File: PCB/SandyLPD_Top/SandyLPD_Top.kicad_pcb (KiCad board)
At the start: 2 copper layers, 30.3 x 23 mm, 22 parts

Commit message: シルク位置調整 #20
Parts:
- moved REF** 5.73 mm to (128.3, 38.3), turned to -90 degrees
- moved REF** 4.31 mm to (145.7, 36.4), turned to 90 degrees
- moved REF** 0.95 mm to (121.0, 38.9)
- moved REF** 0.85 mm to (143.6, 55.0)
- moved REF** 0.83 mm to (143.7, 55.0)
- moved REF** 0.50 mm to (143.7, 39.6)
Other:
- board text added: "L Back"
- board text added: "R Back"
- board text removed: "L 左 Back"
- board text removed: "R 右 Back"
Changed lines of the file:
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@@
 		(locked yes)
 		(layer "F.Cu")
-		(at 143.225342 55.773449)
+		(at 143.645755 55.032837)
 		(property "Reference" "REF**"
 			(at 0 0.5 0)
@@
 		(fp_arc
 			(start 2.475824 -5.107131)
-			(mid 1.4 -5.3)
+			(mid 1.399999 -5.299999)
 			(end 0.555319 -5.993622)
 			(stroke
@@
 		(locked yes)
 		(layer "F.Cu")
-		(at 120.204016 38.385937 -90)
+		(at 121.021287 38.862502 -90)
 		(property "Reference" "REF**"
 			(at 0 0.5 90)
@@
 		(fp_arc
 			(start 2.475824 -5.107131)
-			(mid 1.399999 -5.299999)
+			(mid 1.4 -5.3)
 			(end 0.555319 -5.993622)
 			(stroke
@@
 		(locked yes)
 		(layer "F.Cu")
-		(at 142.225342 38.973449)
+		(at 145.656604 36.370873 90)
 		(property "Reference" "REF**"
-			(at 0 0.5 0)
+			(at 0 0.5 90)
 			(layer "Cmts.User")
 			(effects
@@
 		)
 		(property "Value" "ICON_Screw_Long_Medium"
-			(at 0 -0.5 0)
+			(at 0 -0.5 90)
 			(layer "F.Fab")
 			(effects
@@
 		)
 		(property "Footprint" "locallib:ICON_Screw_Long_Medium"
-			(at 0 0 0)
+			(at 0 0 90)
 			(layer "F.Fab")
 			(hide yes)
@@
 		)
 		(property "Datasheet" ""
-			(at 0 0 0)
+			(at 0 0 90)
 			(layer "F.Fab")
 			(hide yes)
@@
 		)
 		(property "Description" ""
-			(at 0 0 0)
+			(at 0 0 90)
 			(layer "F.Fab")
 			(hide yes)
@@
 		(attr through_hole board_only)
 		(fp_line
-			(start -1.175 -1.6)
-			(end -0.125 -1.6)
+			(start 1.200117 -6.018574)
+			(end 2.000117 -5.318574)
 			(stroke
 				(width 0.06)
@@
 		)
 		(fp_line
-			(start -0.925 -2.05)
-			(end 0.125 -2.05)
+			(start 1.950117 -5.818574)
+			(end 1.200117 -5.568574)
 			(stroke
 				(width 0.06)
@@
 		)
 		(fp_line
-			(start -0.675 -2.5)
-			(end 0.375 -2.5)
+			(start 0.95 -5.55)
+			(end -1.3 -1.5)
 			(stroke
-				(width 0.06)
+				(width 0.12)
 				(type solid)
 			)
@@
 		)
 		(fp_line
-			(start -0.425 -2.95)
-			(end 0.625 -2.95)
+			(start 1.85 -5.1)
+			(end -0.35 -1.1)
 			(stroke
-				(width 0.06)
+				(width 0.12)
 				(type solid)
 			)
@@
 		)
 		(fp_line
-			(start -0.175 -3.45)
-			(end 0.875 -3.45)
+			(start 0.675 -4.95)
+			(end 1.725 -4.95)
 			(stroke
 				(width 0.06)
@@
 		)
 		(fp_line
-			(start 0.125 -3.95)
-			(end 1.175 -3.95)
+			(start 0.375 -4.45)
+			(end 1.425 -4.45)
 			(stroke
 				(width 0.06)
@@
 		)
 		(fp_line
-			(start 0.375 -4.45)
-			(end 1.425 -4.45)
+			(start 0.125 -3.95)
+			(end 1.175 -3.95)
 			(stroke
 				(width 0.06)
@@
 		)
 		(fp_line
-			(start 0.675 -4.95)
-			(end 1.725 -4.95)
+			(start -0.175 -3.45)
+			(end 0.875 -3.45)
 			(stroke
 				(width 0.06)
@@
 		)
 		(fp_line
-			(start 0.95 -5.55)
-			(end -1.3 -1.5)
+			(start -0.425 -2.95)
+			(end 0.625 -2.95)
 			(stroke
-				(width 0.12)
+				(width 0.06)
 				(type solid)
 			)
@@
 		)
 		(fp_line
-			(start 1.200117 -6.018574)
-			(end 2.000117 -5.318574)
+			(start -0.675 -2.5)
+			(end 0.375 -2.5)
 			(stroke
 				(width 0.06)
@@
 		)
 		(fp_line
-			(start 1.85 -5.1)
-			(end -0.35 -1.1)
+			(start -0.925 -2.05)
+			(end 0.125 -2.05)
 			(stroke
-				(width 0.12)
+				(width 0.06)
 				(type solid)
 			)
@@
 		)
 		(fp_line
-			(start 1.950117 -5.818574)
-			(end 1.200117 -5.568574)
+			(start -1.175 -1.6)
+			(end -0.125 -1.6)
 			(stroke
 				(width 0.06)
@@
 		)
 		(fp_arc
-			(start -0.35 -1.1)
-			(mid -0.918136 -1.068963)
-			(end -1.308578 -1.482842)
+			(start 0.665318 -6.21362)
+			(mid 1.74926 -6.077071)
+			(end 2.5615 -5.346425)
 			(stroke
 				(width 0.12)
@@
 		)
 		(fp_arc
-			(start 0.665318 -6.21362)
-			(mid 1.74926 -6.077071)
-			(end 2.5615 -5.346425)
+			(start 2.557784 -5.343159)
+			(mid 2.58557 -5.201266)
+			(end 2.475824 -5.107132)
 			(stroke
 				(width 0.12)
-				(type solid)
+				(type default)
 			)
 			(layer "F.SilkS")
@@
 		(fp_arc
 			(start 2.475824 -5.107131)
-			(mid 1.4 -5.3)
+			(mid 1.399999 -5.299999)
 			(end 0.555319 -5.993622)
 			(stroke
@@
 		)
 		(fp_arc
-			(start 2.557784 -5.343159)
-			(mid 2.58557 -5.201266)
-			(end 2.475824 -5.107132)
+			(start -0.35 -1.1)
+			(mid -0.918136 -1.068963)
+			(end -1.308578 -1.482842)
 			(stroke
 				(width 0.12)
-				(type default)
+				(type solid)
 			)
 			(layer "F.SilkS")
@@
 	)
 	(footprint "locallib:ICON_Screw_Long_Medium"
+		(locked yes)
 		(layer "B.Cu")
-		(at 126.110278 43.573449 180)
+		(at 128.264501 38.267183 -90)
 		(property "Reference" "REF**"
-			(at 0 -0.5 0)
+			(at 0 -0.5 90)
 			(layer "Cmts.User")
 			(effects
@@
 		)
 		(property "Value" "ICON_Screw_Long_Medium"
-			(at 0 0.5 0)
+			(at 0 0.5 90)
 			(layer "B.Fab")
 			(effects
@@
 		)
 		(property "Footprint" "locallib:ICON_Screw_Long_Medium"
-			(at 0 0 0)
+			(at 0 0 90)
 			(layer "B.Fab")
 			(hide yes)
@@
 		)
 		(property "Datasheet" ""
-			(at 0 0 0)
+			(at 0 0 90)
 			(layer "B.Fab")
 			(hide yes)
@@
 		)
 		(property "Description" ""
-			(at 0 0 0)
+			(at 0 0 90)
 			(layer "B.Fab")
 			(hide yes)
@@
 		(attr through_hole board_only)
 		(fp_line
-			(start 2.000117 5.318574)
-			(end 1.200117 6.018574)
+			(start 1.200117 5.568574)
+			(end 1.950117 5.818574)
 			(stroke
 				(width 0.06)
@@
 		)
 		(fp_line
-			(start 1.725 4.95)
-			(end 0.675 4.95)
+			(start 2.000117 5.318574)
+			(end 1.200117 6.018574)
 			(stroke
 				(width 0.06)
@@
 		)
 		(fp_line
-			(start 1.425 4.45)
-			(end 0.375 4.45)
+			(start 1.725 4.95)
+			(end 0.675 4.95)
 			(stroke
 				(width 0.06)
@@
 		)
 		(fp_line
-			(start 1.200117 5.568574)
-			(end 1.950117 5.818574)
+			(start 1.425 4.45)
+			(end 0.375 4.45)
 			(stroke
 				(width 0.06)
@@
 		)
 		(fp_line
-			(start -0.35 1.1)
-			(end 1.85 5.1)
+			(start -1.3 1.5)
+			(end 0.95 5.55)
 			(stroke
 				(width 0.12)
@@
 		)
 		(fp_line
-			(start -1.3 1.5)
-			(end 0.95 5.55)
+			(start -0.35 1.1)
+			(end 1.85 5.1)
 			(stroke
 				(width 0.12)
@@
 		)
 		(fp_arc
-			(start 2.5615 5.346425)
-			(mid 1.74926 6.077071)
-			(end 0.665318 6.21362)
+			(start 0.665318 6.21362)
+			(mid 0.542323 6.113993)
+			(end 0.582958 5.961016)
 			(stroke
 				(width 0.12)
-				(type solid)
+				(type default)
 			)
 			(layer "B.SilkS")
 		)
 		(fp_arc
-			(start 2.475824 5.107132)
-			(mid 2.585576 5.201276)
-			(end 2.557784 5.343159)
+			(start 0.555319 5.993622)
+			(mid 1.399999 5.299999)
+			(end 2.475824 5.107131)
 			(stroke
 				(width 0.12)
-				(type default)
+				(type solid)
 			)
 			(layer "B.SilkS")
 		)
 		(fp_arc
-			(start 0.665318 6.21362)
-			(mid 0.542323 6.113993)
-			(end 0.582958 5.961016)
+			(start 2.5615 5.346425)
+			(mid 1.74926 6.077071)
+			(end 0.665318 6.21362)
 			(stroke
 				(width 0.12)
-				(type default)
+				(type solid)
 			)
 			(layer "B.SilkS")
 		)
 		(fp_arc
-			(start 0.555319 5.993622)
-			(mid 1.399999 5.299999)
-			(end 2.475824 5.107131)
+			(start 2.475824 5.107132)
+			(mid 2.585576 5.201276)
+			(end 2.557784 5.343159)
 			(stroke
 				(width 0.12)
-				(type solid)
+				(type default)
 			)
 			(layer "B.SilkS")
@@
 	(footprint "locallib:ICON_Screw_Long_Medium"
 		(layer "B.Cu")
-		(at 143.672785 39.054699 180)
+		(at 143.672785 39.554699 180)
 		(property "Reference" "REF**"
 			(at 0 -0.5 0)
@@
 	)
 	(footprint "locallib:ICON_Screw_Long_Medium"
+		(locked yes)
 		(layer "B.Cu")
-		(at 144.110278 55.773449 180)
+		(at 143.740072 55.032837 180)
 		(property "Reference" "REF**"
 			(at 0 -0.5 0)
@@
 	)
 	(gr_rect
-		(start 121.06781 42.228405)
-		(end 126.06781 47.228405)
+		(start 121.666329 42.228405)
+		(end 126.666329 47.228405)
 		(stroke
 			(width 0.3)
@@
 	)
 	(gr_rect
-		(start 121.06781 42.228405)
-		(end 126.06781 47.228405)
+		(start 121.666329 42.228405)
+		(end 126.666329 47.228405)
 		(stroke
 			(width 0.3)
@@
 		(layer "F.SilkS")
 	)
-	(gr_text "L 左 Back"
-		(at 143.03031 40.428405 0)
+	(gr_text "L Back"
+		(at 143.99291 40.695596 0)
 		(layer "B.SilkS" knockout)
 		(effects
@@
 		)
 	)
-	(gr_text "R 右 Back"
-		(at 142.73031 40.428405 0)
+	(gr_text "R Back"
+		(at 143.69291 40.695596 0)
 		(layer "F.SilkS" knockout)
 		(effects
@@
 		)
 	)
-	(gr_text "#SandyLP_Duo\nDN0010"
-		(at 132.03031 34.128405 0)
+	(gr_text "#SandyLP_Duo DN0010"
+		(at 131.03031 38.428405 0)
 		(layer "F.SilkS")
 		(effects

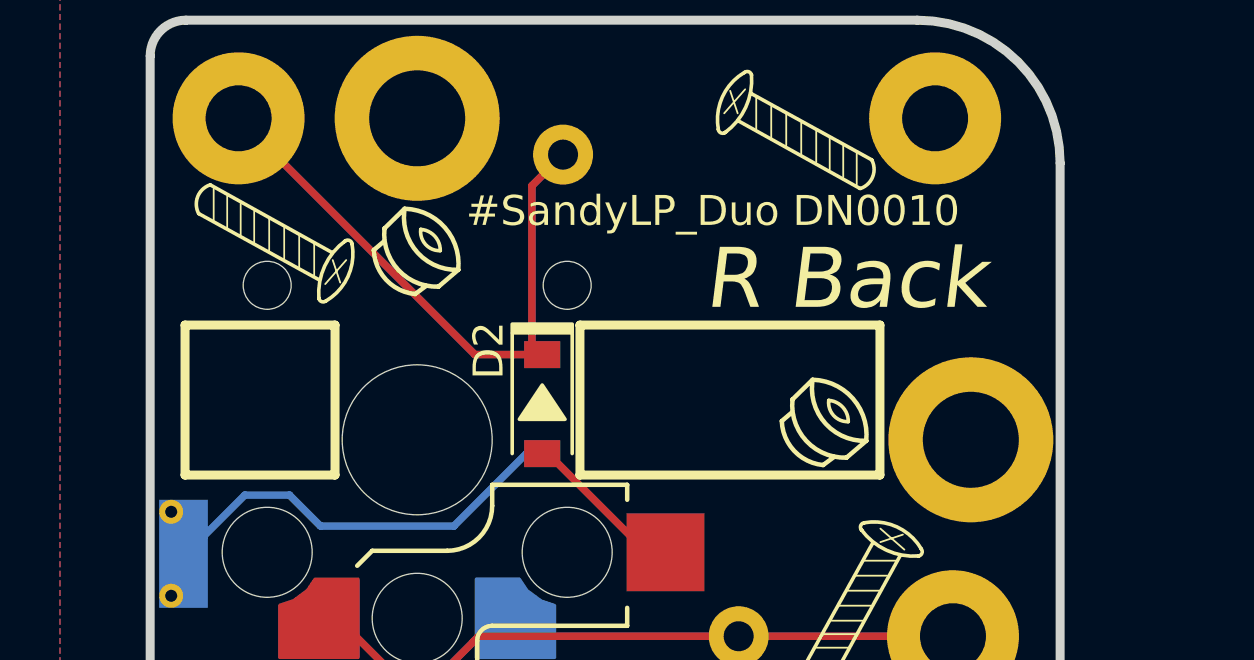
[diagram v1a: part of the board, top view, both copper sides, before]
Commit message: シルク調整
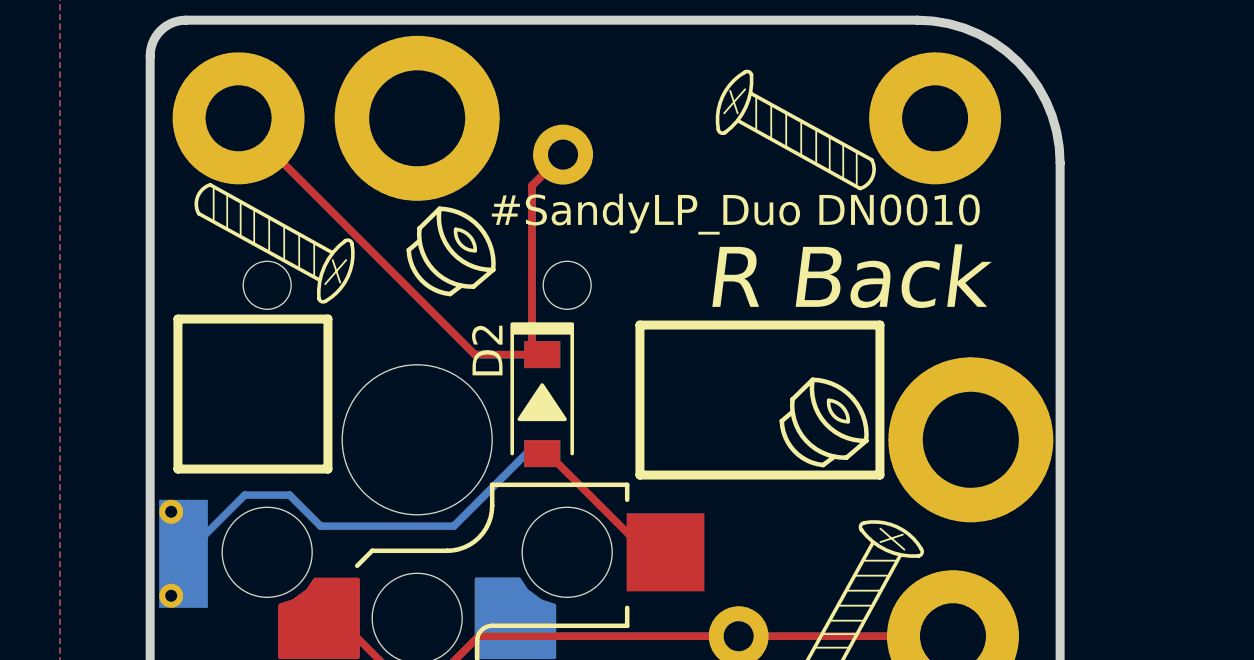
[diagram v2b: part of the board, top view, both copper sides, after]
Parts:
- moved REF** 1.17 mm to (130.6, 39.8) (x2)
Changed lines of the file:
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@@
 		(fp_arc
 			(start 2.475824 -5.107131)
-			(mid 1.399999 -5.299999)
+			(mid 1.4 -5.3)
 			(end 0.555319 -5.993622)
 			(stroke
@@
 		(locked yes)
 		(layer "F.Cu")
-		(at 129.430309 39.828403)
+		(at 130.596024 39.828403)
 		(property "Reference" "REF**"
 			(at 0 -0.5 0)
@@
 		(fp_arc
 			(start 2.475824 -5.107131)
-			(mid 1.4 -5.3)
+			(mid 1.399999 -5.299999)
 			(end 0.555319 -5.993622)
 			(stroke
@@
 		(fp_arc
 			(start 2.475824 -5.107131)
-			(mid 1.399999 -5.299999)
+			(mid 1.4 -5.3)
 			(end 0.555319 -5.993622)
 			(stroke
@@
 		(locked yes)
 		(layer "B.Cu")
-		(at 129.43031 39.828405 180)
+		(at 130.596024 39.828405 180)
 		(property "Reference" "REF**"
 			(at 0 0.5 0)
@@
 	)
 	(gr_rect
-		(start 134.83031 42.228405)
+		(start 136.83031 42.228405)
 		(end 144.83031 47.228405)
 		(stroke
@@
 	)
 	(gr_rect
-		(start 121.666329 42.228405)
-		(end 126.666329 47.228405)
+		(start 121.43031 42.028405)
+		(end 126.43031 47.028405)
 		(stroke
 			(width 0.3)
@@
 	)
 	(gr_rect
-		(start 134.83031 42.228405)
+		(start 136.83031 42.228405)
 		(end 144.83031 47.228405)
 		(stroke
@@
 	)
 	(gr_rect
-		(start 121.666329 42.228405)
-		(end 126.666329 47.228405)
+		(start 121.43031 42.028405)
+		(end 126.43031 47.028405)
 		(stroke
 			(width 0.3)
@@
 	)
 	(gr_text "#SandyLP_Duo DN0010"
-		(at 131.03031 38.428405 0)
+		(at 131.78665 38.428405 0)
 		(layer "F.SilkS")
 		(effects

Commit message: ネジの3Dモデル追加
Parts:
- H1, H2: footprint locallib:MountingHole_2.2mm_M2_Pad_minimal -> locallib:MountingHole_2.2mm_M2_Pad_minimal_L8mm_SlimHead
- H3: renamed from H5; footprint locallib:MountingHole_2.2mm_M2_Pad_minimal -> locallib:MountingHole_2.2mm_M2_Pad_minimal_L8mm_SlimHead
- renumbered H3 to H4, H4 to H5
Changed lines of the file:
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@@
 		(fp_arc
 			(start 2.475824 -5.107131)
-			(mid 1.4 -5.3)
+			(mid 1.399999 -5.299999)
 			(end 0.555319 -5.993622)
 			(stroke
@@
 		(descr "Mounting Hole 2.2mm, M2")
 		(tags "mounting hole 2.2mm m2")
-		(property "Reference" "H3"
+		(property "Reference" "H4"
 			(at 0 -3.2 0)
 			(layer "F.SilkS")
@@
 		(descr "Mounting Hole 2.2mm, M2")
 		(tags "mounting hole 2.2mm m2")
-		(property "Reference" "H4"
+		(property "Reference" "H5"
 			(at 0 -3.2 0)
 			(layer "F.SilkS")
@@
 		)
 	)
-	(footprint "locallib:MountingHole_2.2mm_M2_Pad_minimal"
+	(footprint "locallib:MountingHole_2.2mm_M2_Pad_minimal_L8mm_SlimHead"
 		(layer "F.Cu")
 		(at 147.264792 52.601858)
@@
 			)
 		)
-		(property "Footprint" "locallib:MountingHole_2.2mm_M2_Pad_minimal"
+		(property "Footprint" "locallib:MountingHole_2.2mm_M2_Pad_minimal_L8mm_SlimHead"
 			(at 0 0 0)
 			(layer "F.Fab")
@@
 			(pintype "input")
 		)
+		(model "${KIPRJMOD}/locallib.pretty/CSPSL-ST3W-M2-8_203.STEP"
+			(hide yes)
+			(offset
+				(xyz 0 0 0)
+			)
+			(scale
+				(xyz 1 1 1)
+			)
+			(rotate
+				(xyz 0 0 0)
+			)
+		)
+		(model "${KIPRJMOD}/locallib.pretty/CSPSL-ST3W-M2-8_214.STEP"
+			(offset
+				(xyz 0 0 0)
+			)
+			(scale
+				(xyz 1 1 1)
+			)
+			(rotate
+				(xyz 0 0 0)
+			)
+		)
 	)
-	(footprint "locallib:MountingHole_2.2mm_M2_Pad_minimal"
+	(footprint "locallib:MountingHole_2.2mm_M2_Pad_minimal_L8mm_SlimHead"
 		(layer "F.Cu")
 		(at 123.452272 35.337781)
@@
 			)
 		)
-		(property "Footprint" "locallib:MountingHole_2.2mm_M2_Pad_minimal"
+		(property "Footprint" "locallib:MountingHole_2.2mm_M2_Pad_minimal_L8mm_SlimHead"
 			(at 0 0 0)
 			(layer "F.Fab")
@@
 			(pinfunction "1")
 			(pintype "input")
+		)
+		(model "${KIPRJMOD}/locallib.pretty/CSPSL-ST3W-M2-8_203.STEP"
+			(hide yes)
+			(offset
+				(xyz 0 0 0)
+			)
+			(scale
+				(xyz 1 1 1)
+			)
+			(rotate
+				(xyz 0 0 0)
+			)
+		)
+		(model "${KIPRJMOD}/locallib.pretty/CSPSL-ST3W-M2-8_214.STEP"
+			(offset
+				(xyz 0 0 0)
+			)
+			(scale
+				(xyz 1 1 1)
+			)
+			(rotate
+				(xyz 0 0 0)
+			)
 		)
 	)
@@
 		(fp_arc
 			(start 2.475824 -5.107131)
-			(mid 1.399999 -5.299999)
+			(mid 1.4 -5.3)
 			(end 0.555319 -5.993622)
 			(stroke
@@
 		)
 	)
-	(footprint "locallib:MountingHole_2.2mm_M2_Pad_minimal"
+	(footprint "locallib:MountingHole_2.2mm_M2_Pad_minimal_L8mm_SlimHead"
 		(layer "F.Cu")
 		(at 146.669479 35.337781)
 		(descr "Mounting Hole 2.2mm, M2")
 		(tags "mounting hole 2.2mm m2")
-		(property "Reference" "H5"
+		(property "Reference" "H3"
 			(at 0 -3.2 0)
 			(layer "F.SilkS")
@@
 			)
 		)
-		(property "Footprint" "locallib:MountingHole_2.2mm_M2_Pad_minimal"
+		(property "Footprint" "locallib:MountingHole_2.2mm_M2_Pad_minimal_L8mm_SlimHead"
 			(at 0 0 0)
 			(layer "F.Fab")
@@
 			(pintype "input")
 		)
+		(model "${KIPRJMOD}/locallib.pretty/CSPSL-ST3W-M2-8_203.STEP"
+			(hide yes)
+			(offset
+				(xyz 0 0 0)
+			)
+			(scale
+				(xyz 1 1 1)
+			)
+			(rotate
+				(xyz 0 0 0)
+			)
+		)
+		(model "${KIPRJMOD}/locallib.pretty/CSPSL-ST3W-M2-8_214.STEP"
+			(offset
+				(xyz 0 0 0)
+			)
+			(scale
+				(xyz 1 1 1)
+			)
+			(rotate
+				(xyz 0 0 0)
+			)
+		)
 	)
 	(footprint "locallib:ICON_Screw_Long_Medium"
@@
 		(fp_arc
 			(start 2.475824 -5.107131)
-			(mid 1.4 -5.3)
+			(mid 1.399999 -5.299999)
 			(end 0.555319 -5.993622)
 			(stroke

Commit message: ネジ等の3Dモデル追加
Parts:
- H1, H2, H3: footprint locallib:MountingHole_2.2mm_M2_Pad_minimal_L8mm_SlimHead -> locallib:MountingHole_2.2mm_M2_Pad_minimal_L8mm_SlimHead_L3.5mm_Spacer_Backside
- H4, H5: footprint locallib:MountingHole_M2_Through-hole_tap_THC-0.8-x-2 -> locallib:MountingHole_M2_Through-hole_tap_THC-0.8-1.0-2
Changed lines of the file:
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@@
 		(fp_arc
 			(start 2.475824 -5.107131)
-			(mid 1.399999 -5.299999)
+			(mid 1.4 -5.3)
 			(end 0.555319 -5.993622)
 			(stroke
@@
 		)
 	)
-	(footprint "locallib:MountingHole_M2_Through-hole_tap_THC-0.8-x-2"
+	(footprint "locallib:MountingHole_M2_Through-hole_tap_THC-0.8-1.0-2"
 		(layer "F.Cu")
 		(at 129.405402 35.337781)
@@
 			)
 		)
-		(property "Footprint" "locallib:MountingHole_M2_Through-hole_tap_THC-0.8-x-2"
+		(property "Footprint" "locallib:MountingHole_M2_Through-hole_tap_THC-0.8-1.0-2"
 			(at 0 0 0)
 			(unlocked yes)
@@
 			(layers "*.Cu" "*.Mask")
 			(remove_unused_layers no)
+		)
+		(model "${KIPRJMOD}/locallib.pretty/ThroughHole-Tap_THC-0.8-1.0-2-Fusion.step"
+			(opacity 0.7500)
+			(offset
+				(xyz 0 0 0)
+			)
+			(scale
+				(xyz 1 1 1)
+			)
+			(rotate
+				(xyz 0 0 0)
+			)
 		)
 	)
@@
 		)
 	)
-	(footprint "locallib:MountingHole_M2_Through-hole_tap_THC-0.8-x-2"
+	(footprint "locallib:MountingHole_M2_Through-hole_tap_THC-0.8-1.0-2"
 		(layer "F.Cu")
 		(at 147.860105 46.053415)
@@
 			)
 		)
-		(property "Footprint" "locallib:MountingHole_M2_Through-hole_tap_THC-0.8-x-2"
+		(property "Footprint" "locallib:MountingHole_M2_Through-hole_tap_THC-0.8-1.0-2"
 			(at 0 0 0)
 			(unlocked yes)
@@
 			(remove_unused_layers no)
 		)
+		(model "${KIPRJMOD}/locallib.pretty/ThroughHole-Tap_THC-0.8-1.0-2-Fusion.step"
+			(opacity 0.7500)
+			(offset
+				(xyz 0 0 0)
+			)
+			(scale
+				(xyz 1 1 1)
+			)
+			(rotate
+				(xyz 0 0 0)
+			)
+		)
 	)
-	(footprint "locallib:MountingHole_2.2mm_M2_Pad_minimal_L8mm_SlimHead"
+	(footprint "locallib:MountingHole_2.2mm_M2_Pad_minimal_L8mm_SlimHead_L3.5mm_Spacer_Backside"
 		(layer "F.Cu")
 		(at 147.264792 52.601858)
@@
 			)
 		)
-		(property "Footprint" "locallib:MountingHole_2.2mm_M2_Pad_minimal_L8mm_SlimHead"
+		(property "Footprint" "locallib:MountingHole_2.2mm_M2_Pad_minimal_L8mm_SlimHead_L3.5mm_Spacer_Backside"
 			(at 0 0 0)
 			(layer "F.Fab")
@@
 			)
 		)
+		(model "${KIPRJMOD}/locallib.pretty/Spacer_Circle_M2_D4mm_L3.5mm.step"
+			(opacity 0.5000)
+			(offset
+				(xyz 0 0 -1.6)
+			)
+			(scale
+				(xyz 1 1 1)
+			)
+			(rotate
+				(xyz -180 0 0)
+			)
+		)
 	)
-	(footprint "locallib:MountingHole_2.2mm_M2_Pad_minimal_L8mm_SlimHead"
+	(footprint "locallib:MountingHole_2.2mm_M2_Pad_minimal_L8mm_SlimHead_L3.5mm_Spacer_Backside"
 		(layer "F.Cu")
 		(at 123.452272 35.337781)
@@
 			)
 		)
-		(property "Footprint" "locallib:MountingHole_2.2mm_M2_Pad_minimal_L8mm_SlimHead"
+		(property "Footprint" "locallib:MountingHole_2.2mm_M2_Pad_minimal_L8mm_SlimHead_L3.5mm_Spacer_Backside"
 			(at 0 0 0)
 			(layer "F.Fab")
@@
 			(rotate
 				(xyz 0 0 0)
+			)
+		)
+		(model "${KIPRJMOD}/locallib.pretty/Spacer_Circle_M2_D4mm_L3.5mm.step"
+			(opacity 0.5000)
+			(offset
+				(xyz 0 0 -1.6)
+			)
+			(scale
+				(xyz 1 1 1)
+			)
+			(rotate
+				(xyz -180 0 0)
 			)
 		)
@@
 		(fp_arc
 			(start 2.475824 -5.107131)
-			(mid 1.4 -5.3)
+			(mid 1.399999 -5.299999)
 			(end 0.555319 -5.993622)
 			(stroke
@@
 		)
 	)
-	(footprint "locallib:MountingHole_2.2mm_M2_Pad_minimal_L8mm_SlimHead"
+	(footprint "locallib:MountingHole_2.2mm_M2_Pad_minimal_L8mm_SlimHead_L3.5mm_Spacer_Backside"
 		(layer "F.Cu")
 		(at 146.669479 35.337781)
@@
 			)
 		)
-		(property "Footprint" "locallib:MountingHole_2.2mm_M2_Pad_minimal_L8mm_SlimHead"
+		(property "Footprint" "locallib:MountingHole_2.2mm_M2_Pad_minimal_L8mm_SlimHead_L3.5mm_Spacer_Backside"
 			(at 0 0 0)
 			(layer "F.Fab")
@@
 			)
 		)
+		(model "${KIPRJMOD}/locallib.pretty/Spacer_Circle_M2_D4mm_L3.5mm.step"
+			(opacity 0.5000)
+			(offset
+				(xyz 0 0 -1.6)
+			)
+			(scale
+				(xyz 1 1 1)
+			)
+			(rotate
+				(xyz -180 0 0)
+			)
+		)
 	)
 	(footprint "locallib:ICON_Screw_Long_Medium"
@@
 		(fp_arc
 			(start 2.475824 -5.107131)
-			(mid 1.399999 -5.299999)
+			(mid 1.4 -5.3)
 			(end 0.555319 -5.993622)
 			(stroke
